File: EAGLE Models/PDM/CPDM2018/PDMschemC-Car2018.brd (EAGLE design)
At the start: 82.5 x 63.5 mm, 26 parts

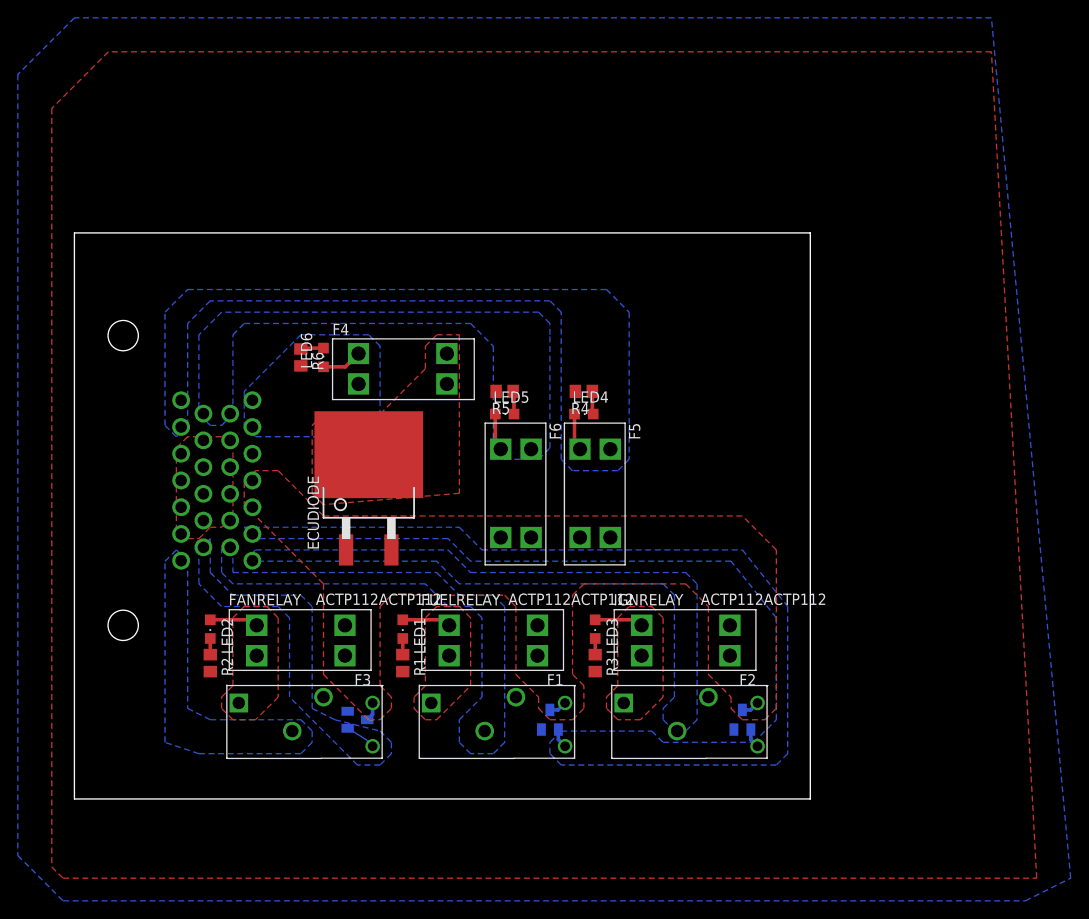
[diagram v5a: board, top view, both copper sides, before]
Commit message: Modified traces
Rerouted traces to remove sharp corners and to make them thicker. GND planes were removed because of complications with ratsnest
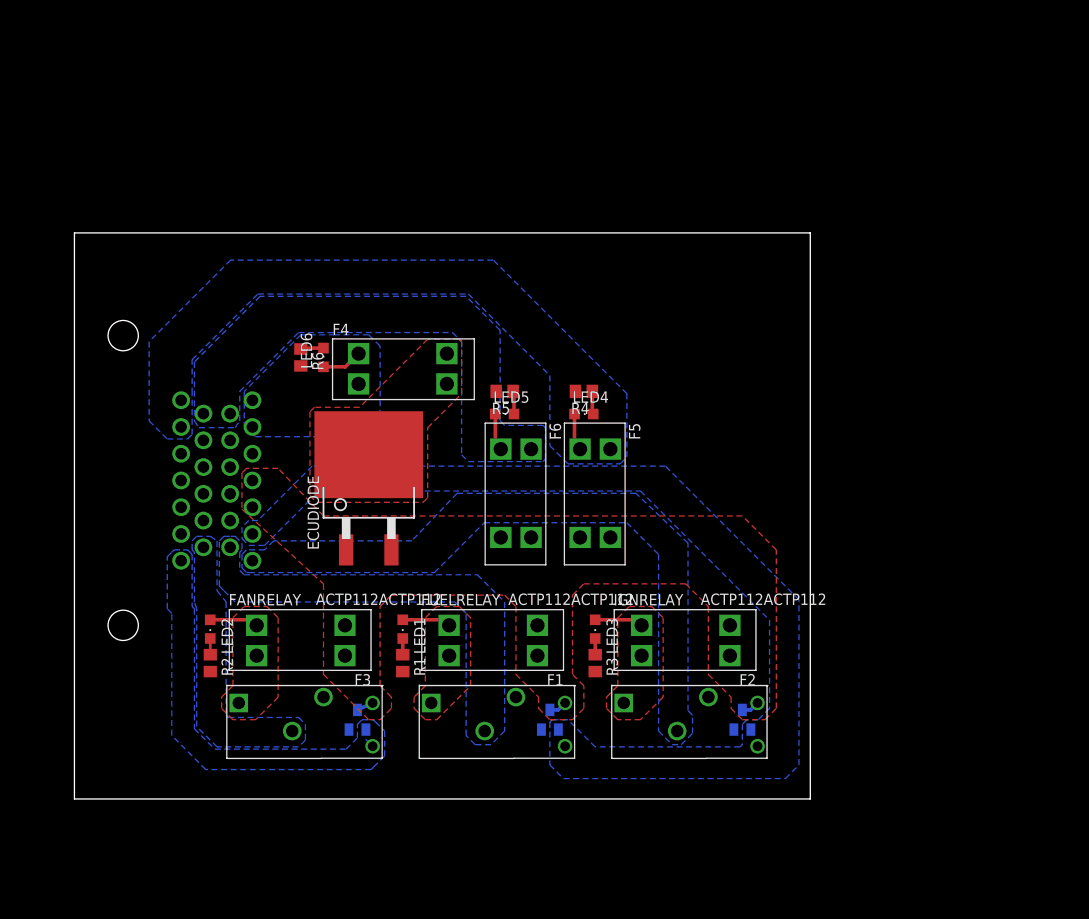
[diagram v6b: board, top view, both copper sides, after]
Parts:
- turned U$7 to 0 degrees
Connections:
- net A23: now also U$1.B26; no longer U$1.B19
- net FAN: now also U$1.B19; no longer U$1.B26
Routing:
- net KILLSW: track 5.49 -> 0.00 mm
- net A23: track 3.47 -> 1.06 mm
- added copper zone on layer 1, net N$9
- removed copper zone on layer 1, net GND
- removed copper zone on layer 1, net N$11
- removed copper zone on layer 16, net N$12
- removed copper zone on layer 1, net N$13

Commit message: Added GND plane
Included the ground plane to board layout.
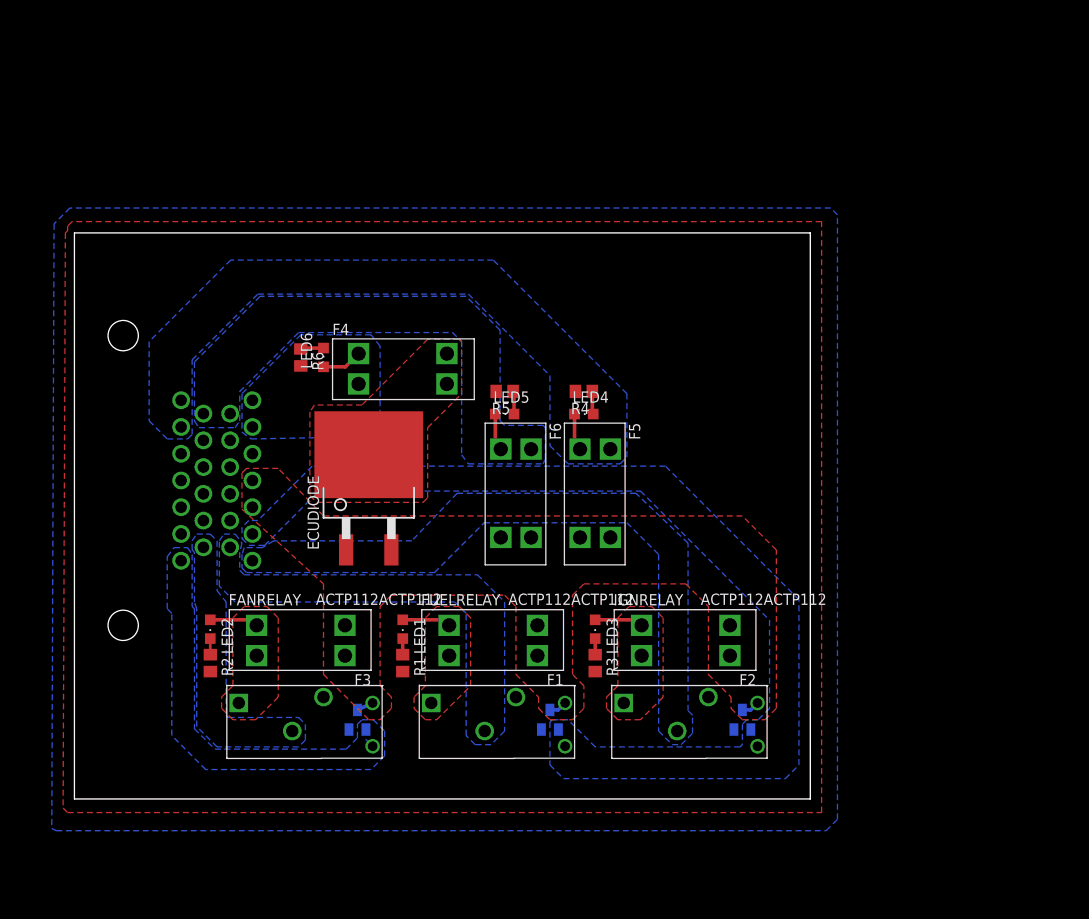
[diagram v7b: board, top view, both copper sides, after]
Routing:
- added copper zone on layer 1, net GND
- added copper zone on layer 16, net GND
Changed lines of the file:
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@@
 <vertex x="13.208" y="27.94"/>
 <vertex x="13.208" y="28.956"/>
-<vertex x="13.716" y="29.464"/>
-<vertex x="15.24" y="29.464"/>
+<vertex x="13.716" y="29.718"/>
+<vertex x="15.24" y="29.718"/>
 </polygon>
 </signal>
@@
 <contactref element="U$1" pad="B7"/>
 <polygon width="0.1524" layer="16">
-<vertex x="19.558" y="25.4"/>
+<vertex x="19.304" y="25.4"/>
 <vertex x="40.386" y="25.4"/>
 <vertex x="45.974" y="30.988"/>
@@
 <vertex x="37.846" y="28.956"/>
 <vertex x="22.352" y="28.956"/>
-<vertex x="21.336" y="27.94"/>
-<vertex x="19.304" y="27.94"/>
+<vertex x="21.082" y="28.194"/>
+<vertex x="19.05" y="28.194"/>
 <vertex x="18.796" y="27.432"/>
 <vertex x="18.796" y="25.908"/>
-<vertex x="19.304" y="25.4"/>
 </polygon>
 </signal>
@@
 <contactref element="U$1" pad="B13"/>
 <polygon width="0.1524" layer="16">
-<vertex x="17.526" y="29.464"/>
-<vertex x="18.034" y="29.464"/>
+<vertex x="16.764" y="29.718"/>
+<vertex x="18.034" y="29.718"/>
 <vertex x="18.796" y="28.702"/>
-<vertex x="18.796" y="27.94"/>
 <vertex x="18.542" y="27.686"/>
 <vertex x="18.542" y="25.654"/>
@@
 <vertex x="42.672" y="22.098"/>
 <vertex x="18.034" y="22.098"/>
-<vertex x="16.764" y="23.368"/>
-<vertex x="16.51" y="23.622"/>
 <vertex x="16.256" y="23.876"/>
 <vertex x="16.256" y="28.956"/>
-<vertex x="16.51" y="29.21"/>
-<vertex x="16.764" y="29.464"/>
 </polygon>
 </signal>
@@
 <wire x1="11.43" y1="29.21" x2="11.45" y2="29.21" width="0.1524" layer="1"/>
 <wire x1="11.45" y1="29.21" x2="11.97" y2="29.73" width="0.1524" layer="1"/>
-<wire x1="47.31" y1="45.72" x2="56.2" y2="45.72" width="0" layer="19" extent="1-1"/>
-<wire x1="25.4" y1="48.58" x2="47.31" y2="45.72" width="0" layer="19" extent="1-1"/>
-<wire x1="17.47" y1="40.23" x2="25.4" y2="48.58" width="0" layer="19" extent="1-1"/>
-<wire x1="14.47" y1="40.23" x2="17.47" y2="40.23" width="0" layer="19" extent="1-1"/>
-<wire x1="11.97" y1="38.73" x2="14.47" y2="40.23" width="0" layer="19" extent="1-1"/>
-<wire x1="14.47" y1="37.23" x2="11.97" y2="38.73" width="0" layer="19" extent="1-1"/>
-<wire x1="11.97" y1="35.73" x2="14.47" y2="37.23" width="0" layer="19" extent="1-1"/>
-<wire x1="14.47" y1="34.23" x2="11.97" y2="35.73" width="0" layer="19" extent="1-1"/>
-<wire x1="11.97" y1="32.73" x2="14.47" y2="34.23" width="0" layer="19" extent="1-1"/>
-<wire x1="14.47" y1="31.23" x2="11.97" y2="32.73" width="0" layer="19" extent="1-1"/>
-<wire x1="11.97" y1="29.73" x2="14.47" y2="31.23" width="0" layer="19" extent="1-1"/>
-<wire x1="17.47" y1="37.23" x2="17.47" y2="40.23" width="0" layer="19" extent="1-1"/>
-<wire x1="17.47" y1="34.23" x2="14.47" y2="34.23" width="0" layer="19" extent="1-1"/>
-<wire x1="17.47" y1="31.23" x2="14.47" y2="31.23" width="0" layer="19" extent="1-1"/>
-<wire x1="15.24" y1="14.29" x2="11.43" y2="29.21" width="0" layer="19" extent="1-1"/>
-<wire x1="36.83" y1="14.29" x2="15.24" y2="14.29" width="0" layer="19" extent="1-1"/>
-<wire x1="58.42" y1="14.29" x2="36.83" y2="14.29" width="0" layer="19" extent="1-1"/>
+<polygon width="0.1524" layer="16" rank="6">
+<vertex x="-2.286" y="64.516"/>
+<vertex x="-2.54" y="-3.302"/>
+<vertex x="-2.032" y="-3.556"/>
+<vertex x="84.328" y="-3.556"/>
+<vertex x="85.598" y="-2.286"/>
+<vertex x="85.598" y="65.532"/>
+<vertex x="84.836" y="66.294"/>
+<vertex x="-0.508" y="66.294"/>
+</polygon>
+<polygon width="0.1524" layer="1" rank="6">
+<vertex x="-1.016" y="63.5"/>
+<vertex x="-1.27" y="-1.016"/>
+<vertex x="-0.762" y="-1.524"/>
+<vertex x="83.82" y="-1.524"/>
+<vertex x="83.82" y="64.77"/>
+<vertex x="-0.254" y="64.77"/>
+<vertex x="-0.762" y="64.262"/>
+<vertex x="-0.762" y="63.754"/>
+</polygon>
 </signal>
 <signal name="DAQ">
@@
 <contactref element="U$1" pad="B1"/>
 <contactref element="U$1" pad="B2"/>
-<polygon width="0.1524" layer="16">
-<vertex x="19.05" y="44.45"/>
-<vertex x="19.05" y="41.91"/>
-<vertex x="20.32" y="40.64"/>
+<wire x1="27.94" y1="48.48" x2="30.3952" y2="48.48" width="0.4064" layer="1"/>
+<wire x1="30.3952" y1="48.48" x2="31.877" y2="49.9618" width="0.4064" layer="1"/>
+<polygon width="0.1524" layer="16">
+<vertex x="18.796" y="45.466"/>
+<vertex x="18.796" y="41.148"/>
+<vertex x="19.812" y="40.386"/>
 <vertex x="33.02" y="40.64"/>
 <vertex x="34.29" y="41.91"/>
 <vertex x="34.29" y="50.8"/>
-<vertex x="33.02" y="52.07"/>
-<vertex x="29.21" y="52.07"/>
+<vertex x="33.274" y="52.07"/>
 <vertex x="25.4" y="52.07"/>
-<vertex x="19.05" y="45.72"/>
-</polygon>
-<wire x1="27.94" y1="48.48" x2="30.3952" y2="48.48" width="0.4064" layer="1"/>
-<wire x1="30.3952" y1="48.48" x2="31.877" y2="49.9618" width="0.4064" layer="1"/>
+</polygon>
 </signal>
 <signal name="SH/B">
@@
 <vertex x="43.434" y="51.308"/>
 <vertex x="43.434" y="38.608"/>
-<vertex x="44.196" y="37.846"/>
-<vertex x="52.578" y="37.846"/>
+<vertex x="44.196" y="37.592"/>
+<vertex x="52.578" y="37.592"/>
 <vertex x="52.832" y="38.1"/>
 <vertex x="52.832" y="41.656"/>
@@
 <vertex x="43.18" y="51.562"/>
 <vertex x="39.624" y="51.562"/>
-<vertex x="32.004" y="43.942"/>
-<vertex x="26.924" y="43.942"/>
+<vertex x="32.258" y="44.196"/>
+<vertex x="26.924" y="44.196"/>
 <vertex x="26.416" y="43.434"/>
 </polygon>
@@
 <contactref element="U$1" pad="B26"/>
 <polygon width="0.1524" layer="16">
-<vertex x="12.192" y="27.94"/>
-<vertex x="12.7" y="27.94"/>
-<vertex x="12.954" y="27.686"/>
+<vertex x="11.176" y="28.194"/>
+<vertex x="12.7" y="28.194"/>
 <vertex x="13.208" y="27.432"/>
 <vertex x="13.208" y="21.59"/>
@@
 <vertex x="32.258" y="8.89"/>
 <vertex x="33.528" y="8.89"/>
-<vertex x="33.782" y="8.636"/>
-<vertex x="34.544" y="7.874"/>
 <vertex x="34.798" y="7.62"/>
-<vertex x="34.798" y="5.08"/>
 <vertex x="34.798" y="4.826"/>
-<vertex x="34.036" y="4.064"/>
-<vertex x="33.782" y="3.81"/>
-<vertex x="33.528" y="3.556"/>
 <vertex x="33.274" y="3.302"/>
-<vertex x="14.986" y="3.302"/>
 <vertex x="14.732" y="3.302"/>
 <vertex x="10.922" y="7.112"/>
@@
 <vertex x="10.414" y="21.336"/>
 <vertex x="10.414" y="27.178"/>
-<vertex x="10.922" y="27.686"/>
-<vertex x="11.176" y="27.94"/>
-</polygon>
-</signal>
+</polygon>
+</signal>

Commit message: Added holes to CPDM
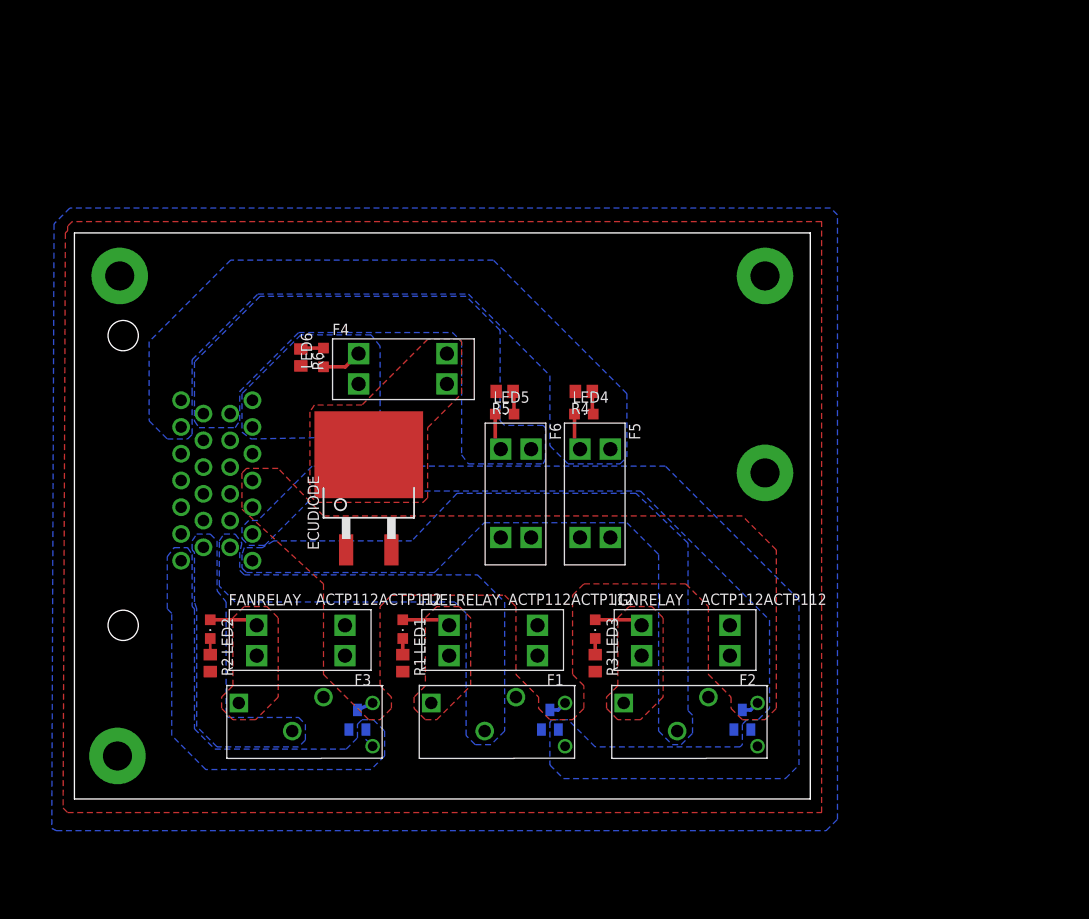
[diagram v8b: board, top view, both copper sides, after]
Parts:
- added H1, H2, H3, H4: MOUNT-PAD-ROUND#4-40-PAD, holes:#4-40-PAD-ROUND
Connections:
- net GND: now also H1.P$1, H2.P$1, H3.P$1, H4.P$1
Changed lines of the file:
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@@
 <?xml version="1.0" encoding="utf-8"?>
 <!DOCTYPE eagle SYSTEM "eagle.dtd">
-<eagle version="8.3.2">
+<eagle version="8.3.0">
 <drawing>
 <settings>
@@
 <element name="R1" library="resistor" library_urn="urn:adsk.eagle:library:348" package="R0805" package3d_urn="urn:adsk.eagle:package:26059/1" value="1K" x="36.83" y="15.24" rot="R270"/>
 <element name="LED1" library="led" library_urn="urn:adsk.eagle:library:259" package="CHIPLED_0805" package3d_urn="urn:adsk.eagle:package:15821/1" value="" x="36.83" y="19.05" rot="R180"/>
+<element name="H1" library="holes" package="#4-40-PAD-ROUND" value="MOUNT-PAD-ROUND#4-40-PAD" x="4.826" y="4.826"/>
+<element name="H2" library="holes" package="#4-40-PAD-ROUND" value="MOUNT-PAD-ROUND#4-40-PAD" x="5.08" y="58.674"/>
+<element name="H3" library="holes" package="#4-40-PAD-ROUND" value="MOUNT-PAD-ROUND#4-40-PAD" x="77.47" y="58.674"/>
+<element name="H4" library="holes" package="#4-40-PAD-ROUND" value="MOUNT-PAD-ROUND#4-40-PAD" x="77.47" y="36.576"/>
 </elements>
 <signals>
@@
 <vertex x="-0.762" y="63.754"/>
 </polygon>
+<contactref element="H1" pad="P$1"/>
+<contactref element="H2" pad="P$1"/>
+<contactref element="H3" pad="P$1"/>
+<contactref element="H4" pad="P$1"/>
 </signal>
 <signal name="DAQ">
